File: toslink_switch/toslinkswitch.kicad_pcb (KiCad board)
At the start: 2 copper layers, 125.1 x 45.3 mm, 47 parts, among them IC1 ATMEGA48A-AU, IC2 SN74CBT3251, J1 CONN_02X03, J2 USB_OTG, SW2 INPUT_CYCL_SW, SW3 SW_DIP_x02

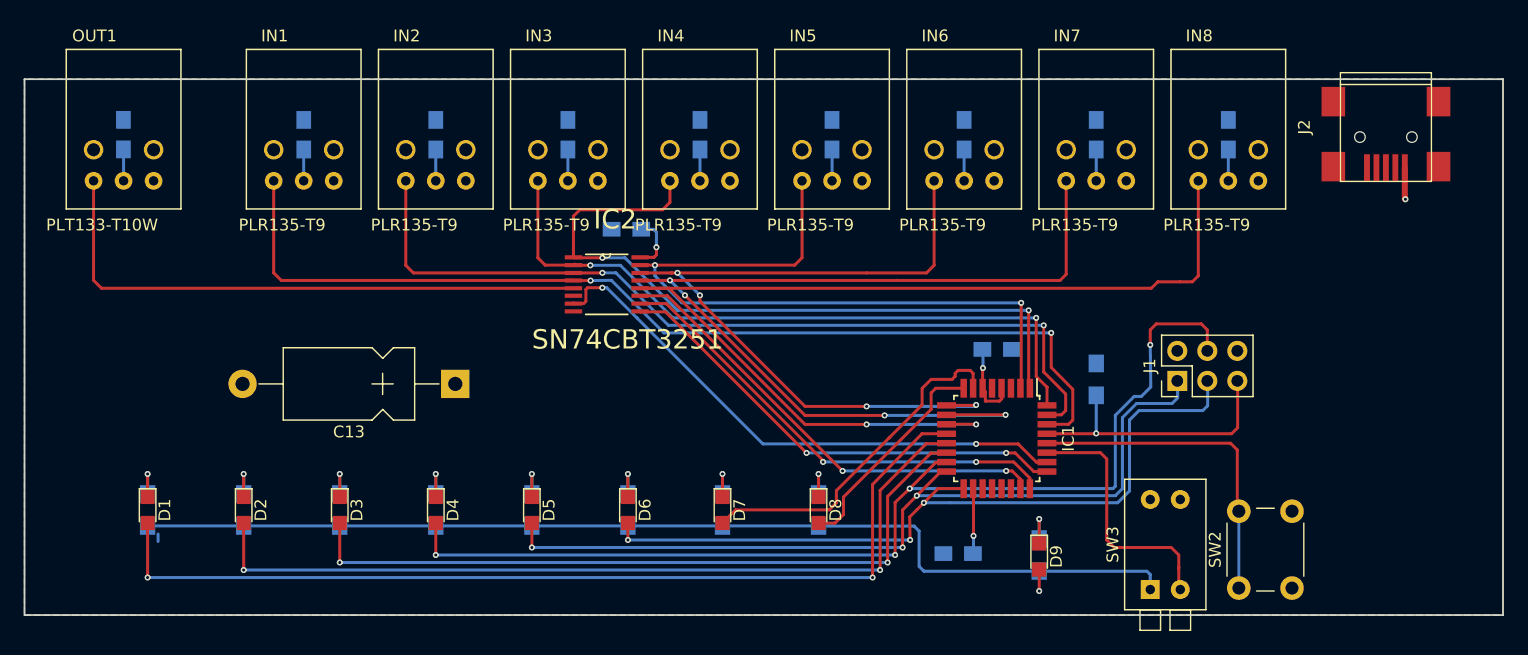
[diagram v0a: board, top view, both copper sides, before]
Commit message: add attiny for IR reciver functionality (https://blog.turboturbo.net/2016/10/01/ir-pc-power-on-quick-n-dirty/)
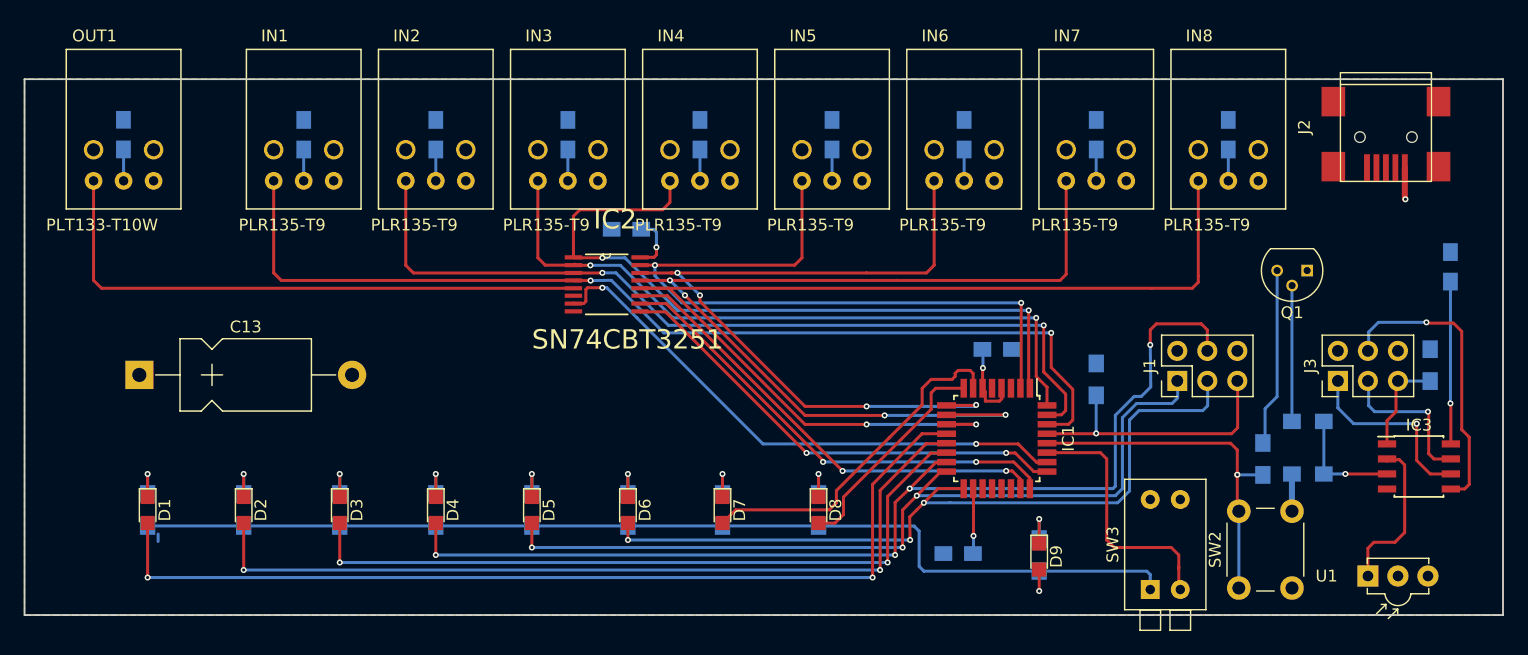
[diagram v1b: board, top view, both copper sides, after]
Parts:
- added C14: 100n, Capacitors_SMD:C_0805_HandSoldering, B.Cu at (181.4, 84.8)
- added IC3: ATTINY85-20SU, Housings_SOIC:SOIC-8_3.9x4.9mm_Pitch1.27mm, F.Cu at (178.7, 101.7)
- added J3: CONN_02X03, Pin_Headers:Pin_Header_Straight_2x03_Pitch2.54mm, F.Cu at (171.8, 94.5)
- added Q1: PN2222A, TO_SOT_Packages_THT:TO-92_Molded_Narrow, F.Cu at (169.2, 85.2)
- added R11: 47, Resistors_SMD:R_0805_HandSoldering, B.Cu at (169.3, 97.9)
- added R12: 47, Resistors_SMD:R_0805_HandSoldering, B.Cu at (165.5, 101.1)
- added R13: 1k, Resistors_SMD:R_0805_HandSoldering, B.Cu at (169.3, 102.4)
- added R14: 10k, Resistors_SMD:R_0805_HandSoldering, B.Cu at (179.6, 93.2)
- added U1: TSOP382xx, Opto-Devices:IRReceiver_Vishay_MINICAST-3pin, F.Cu at (174.4, 111.0)
- moved C13 26.7 mm to (70.4, 94.0), turned to 0 degrees
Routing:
- net Net-(IC3-Pad5): track 0.00 -> 25.1 mm, vias 0 -> 1
- net Net-(IC3-Pad6): track 0.00 -> 16.1 mm, vias 0 -> 1
- net Net-(Q1-Pad3): track 0.00 -> 15.2 mm
- net Net-(C14-Pad1): track 0.00 -> 13.8 mm, vias 0 -> 1
- net IR: track 0.00 -> 13.5 mm
- net Net-(IC3-Pad7): track 0.00 -> 13.1 mm, vias 0 -> 1
- net Net-(Q1-Pad2): track 0.00 -> 11.5 mm
- net IRSWSIG: track 0.00 -> 9.79 mm, vias 0 -> 1
- net Net-(IC3-Pad1): track 0.00 -> 8.57 mm
- net GND: track 0.34 -> 3.50 mm
- net TACT: track 28.1 -> 30.3 mm, vias 0 -> 1
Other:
- net class Default: trace_width 0.508 -> 0.254

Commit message: put some mounting holes where we still have space, we can cleanup later
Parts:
- added REF**: MountingHole_4mm, Mounting_Holes:MountingHole_4mm, F.Cu at (175.3, 82.9)
- added REF**: MountingHole_4mm, Mounting_Holes:MountingHole_4mm, F.Cu at (97.9, 93.5)
- added REF**: MountingHole_4mm, Mounting_Holes:MountingHole_4mm, F.Cu at (76.6, 82.2)
- added REF**: MountingHole_4mm, Mounting_Holes:MountingHole_4mm, F.Cu at (66.3, 108.0)
- added REF**: MountingHole_4mm, Mounting_Holes:MountingHole_4mm, F.Cu at (154.9, 82.7)
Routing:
- net (no net): track 0.64 -> 0.00 mm
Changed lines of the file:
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@@
     (links 128)
     (no_connects 0)
-    (area 60.630999 68.885999 185.876001 114.375001)
+    (area 60.630999 64.47 185.876001 115.966001)
     (thickness 1.6)
     (drawings 8)
-    (tracks 504)
+    (tracks 503)
     (zones 0)
-    (modules 56)
+    (modules 61)
     (nets 65)
   )
@@
       (net 42 VCC))
   )
+  (module Mounting_Holes:MountingHole_4mm (layer F.Cu)
+    (at 175.3235 82.931)
+    (descr "Mounting Hole 4mm, no annular")
+    (tags "mounting hole 4mm no annular")
+    (fp_text reference REF** (at 0 -5) (layer F.SilkS)
+      (effects (font (size 1 1) (thickness 0.15)))
+    )
+    (fp_text value MountingHole_4mm (at 0 5) (layer F.Fab)
+      (effects (font (size 1 1) (thickness 0.15)))
+    )
+    (fp_circle (center 0 0) (end 4 0) (layer Cmts.User) (width 0.15))
+    (fp_circle (center 0 0) (end 4.25 0) (layer F.CrtYd) (width 0.05))
+    (pad 1 np_thru_hole circle (at 0 0) (size 4 4) (drill 4) (layers *.Cu *.Mask))
+  )
+  (module Mounting_Holes:MountingHole_4mm (layer F.Cu)
+    (at 97.8535 93.5355)
+    (descr "Mounting Hole 4mm, no annular")
+    (tags "mounting hole 4mm no annular")
+    (fp_text reference REF** (at 0 -5) (layer F.SilkS)
+      (effects (font (size 1 1) (thickness 0.15)))
+    )
+    (fp_text value MountingHole_4mm (at 0 5) (layer F.Fab)
+      (effects (font (size 1 1) (thickness 0.15)))
+    )
+    (fp_circle (center 0 0) (end 4 0) (layer Cmts.User) (width 0.15))
+    (fp_circle (center 0 0) (end 4.25 0) (layer F.CrtYd) (width 0.05))
+    (pad 1 np_thru_hole circle (at 0 0) (size 4 4) (drill 4) (layers *.Cu *.Mask))
+  )
+  (module Mounting_Holes:MountingHole_4mm (layer F.Cu)
+    (at 76.581 82.169)
+    (descr "Mounting Hole 4mm, no annular")
+    (tags "mounting hole 4mm no annular")
+    (fp_text reference REF** (at 0 -5) (layer F.SilkS)
+      (effects (font (size 1 1) (thickness 0.15)))
+    )
+    (fp_text value MountingHole_4mm (at 0 5) (layer F.Fab)
+      (effects (font (size 1 1) (thickness 0.15)))
+    )
+    (fp_circle (center 0 0) (end 4 0) (layer Cmts.User) (width 0.15))
+    (fp_circle (center 0 0) (end 4.25 0) (layer F.CrtYd) (width 0.05))
+    (pad 1 np_thru_hole circle (at 0 0) (size 4 4) (drill 4) (layers *.Cu *.Mask))
+  )
+  (module Mounting_Holes:MountingHole_4mm (layer F.Cu)
+    (at 66.294 107.95)
+    (descr "Mounting Hole 4mm, no annular")
+    (tags "mounting hole 4mm no annular")
+    (fp_text reference REF** (at 0 -5) (layer F.SilkS)
+      (effects (font (size 1 1) (thickness 0.15)))
+    )
+    (fp_text value MountingHole_4mm (at 0 5) (layer F.Fab)
+      (effects (font (size 1 1) (thickness 0.15)))
+    )
+    (fp_circle (center 0 0) (end 4 0) (layer Cmts.User) (width 0.15))
+    (fp_circle (center 0 0) (end 4.25 0) (layer F.CrtYd) (width 0.05))
+    (pad 1 np_thru_hole circle (at 0 0) (size 4 4) (drill 4) (layers *.Cu *.Mask))
+  )
+  (module Mounting_Holes:MountingHole_4mm (layer F.Cu)
+    (at 154.94 82.677)
+    (descr "Mounting Hole 4mm, no annular")
+    (tags "mounting hole 4mm no annular")
+    (fp_text reference REF** (at 0 -5) (layer F.SilkS)
+      (effects (font (size 1 1) (thickness 0.15)))
+    )
+    (fp_text value MountingHole_4mm (at 0 5) (layer F.Fab)
+      (effects (font (size 1 1) (thickness 0.15)))
+    )
+    (fp_circle (center 0 0) (end 4 0) (layer Cmts.User) (width 0.15))
+    (fp_circle (center 0 0) (end 4.25 0) (layer F.CrtYd) (width 0.05))
+    (pad 1 np_thru_hole circle (at 0 0) (size 4 4) (drill 4) (layers *.Cu *.Mask))
+  )
   (gr_text https://circuit-board.de/forum/index.php/Thread/19096 (at 149.733 84.963) (layer B.Mask)
     (effects (font (size 1.5 1.5) (thickness 0.3)) (justify mirror))
@@
   (gr_line (start 60.706 68.961) (end 60.706 114.3) (angle 90) (layer Edge.Cuts) (width 0.15))
   (gr_line (start 185.801 68.961) (end 185.801 114.3) (angle 90) (layer Edge.Cuts) (width 0.15))
-  (segment (start 72.009 107.442) (end 72.009 108.077) (width 0.254) (layer B.Cu) (net 0))
   (segment (start 145.669 95.009) (end 145.669 88.519) (width 0.254) (layer F.Cu) (net 1))
   (segment (start 111.506 84.074) (end 115.951 88.519) (width 0.254) (layer B.Cu) (net 1))

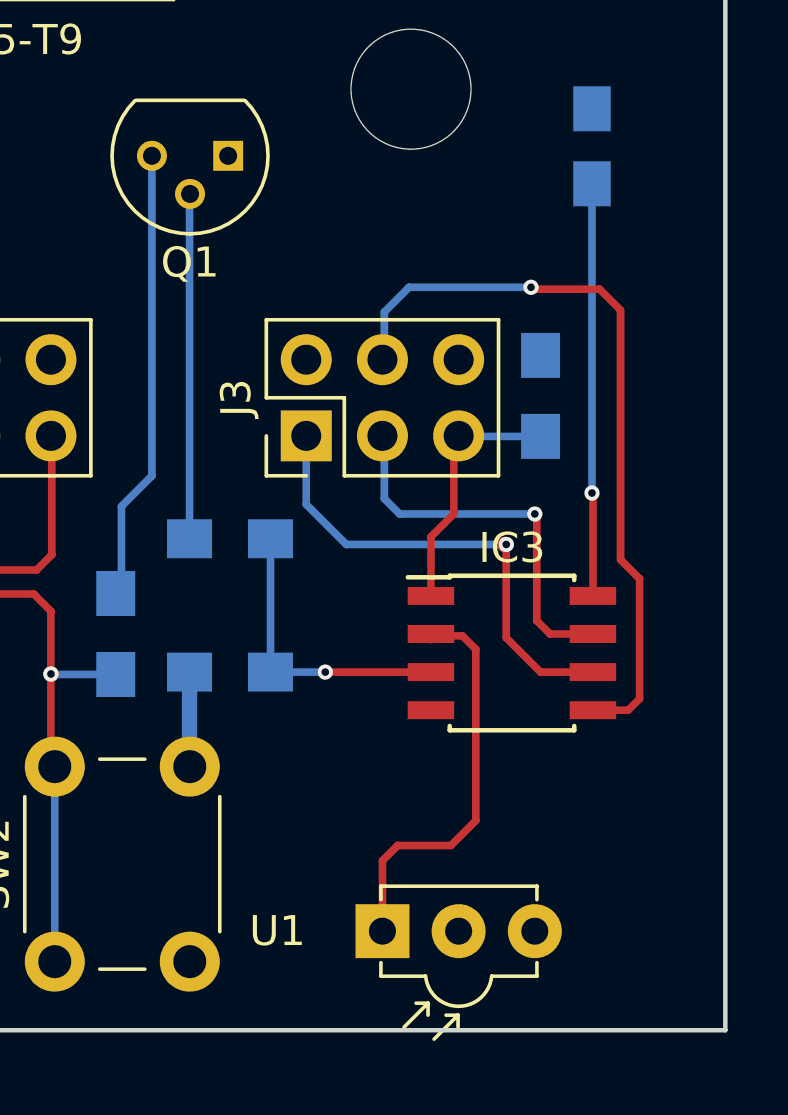
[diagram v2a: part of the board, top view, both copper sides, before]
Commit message: small tweaks to ic3 location
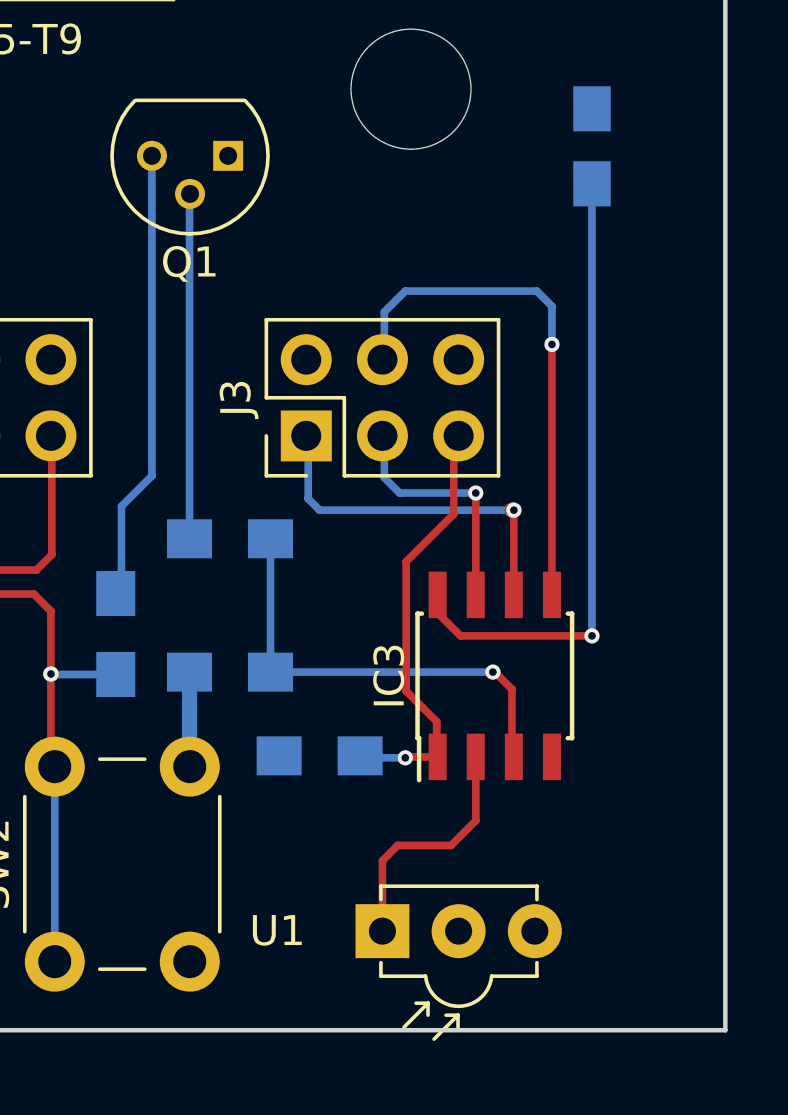
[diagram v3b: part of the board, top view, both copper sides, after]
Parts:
- moved R14 14.1 mm to (172.3, 105.2), turned to 180 degrees
- moved IC3 0.95 mm to (178.1, 102.5), turned to 90 degrees
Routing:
- net Net-(IC3-Pad5): track 25.1 -> 17.4 mm
- net Net-(C14-Pad1): track 13.8 -> 21.2 mm
- net Net-(IC3-Pad1): track 8.57 -> 14.8 mm, vias 0 -> 1
- net IR: track 13.5 -> 8.14 mm
- net IRSWSIG: track 9.79 -> 15.0 mm
- net Net-(IC3-Pad7): track 13.1 -> 8.31 mm
- net Net-(IC3-Pad6): track 16.1 -> 12.1 mm

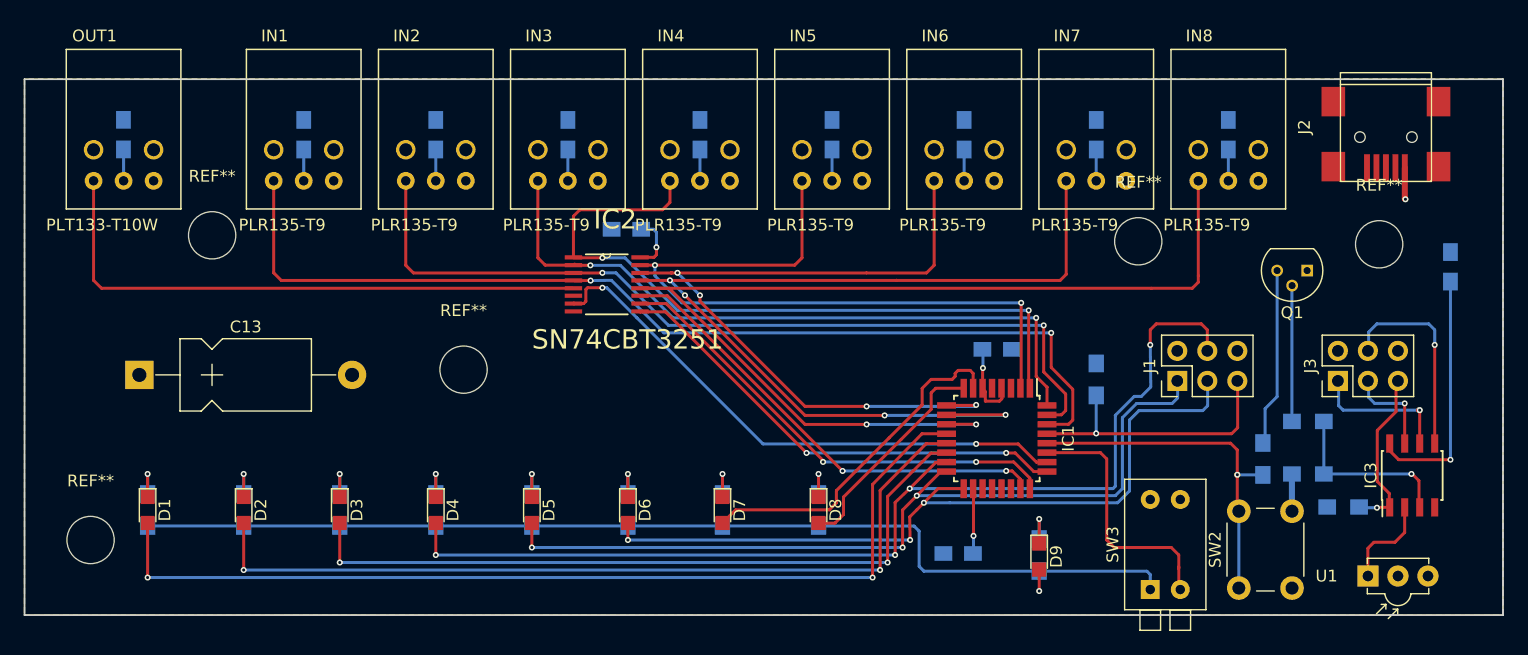
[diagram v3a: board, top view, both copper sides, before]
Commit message: move led's close to the edge of the board
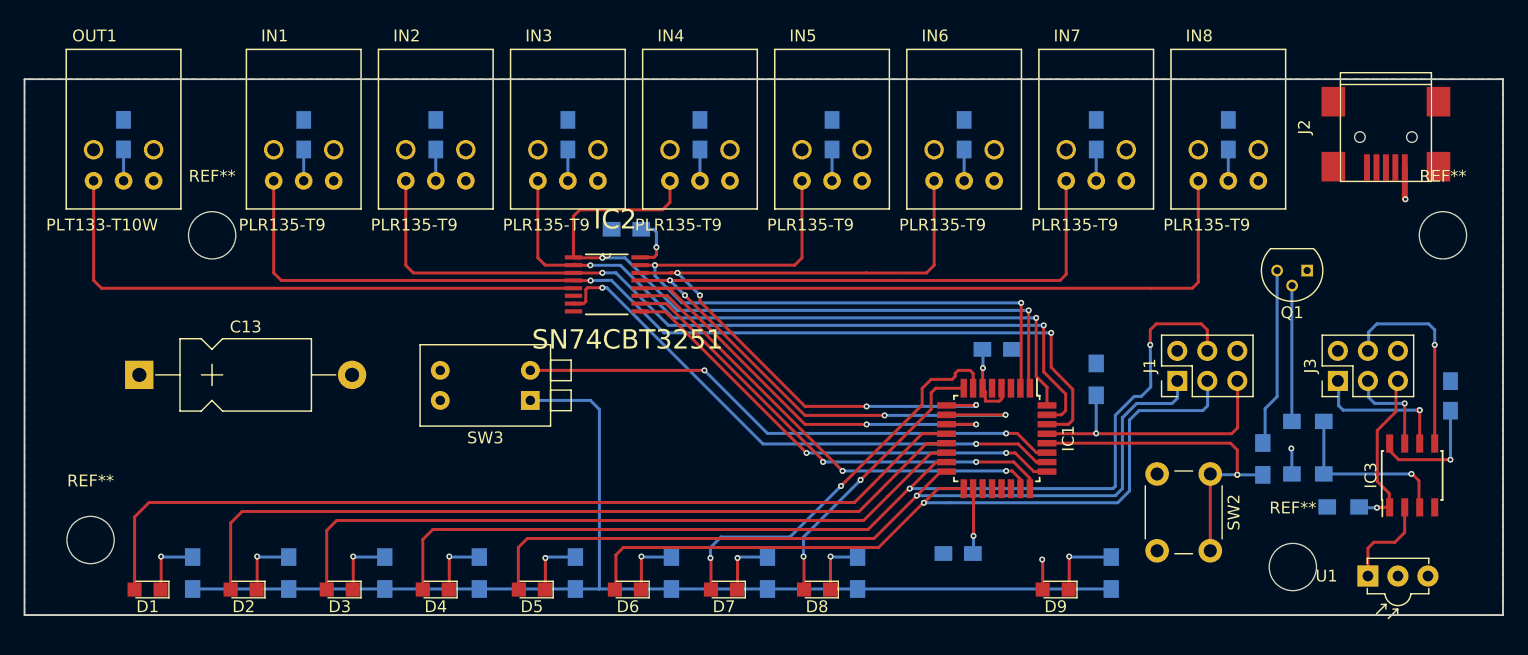
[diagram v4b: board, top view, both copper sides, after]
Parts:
- removed the REF** at (97.9, 93.5)
- moved SW3 54.8 mm to (103.5, 96.1), turned to 180 degrees
- moved REF** 30.5 mm to (168.0, 110.2)
- moved C14 10.9 mm to (181.4, 95.8)
- moved SW2 9.95 mm to (161.0, 102.4), turned to 270 degrees
- moved D7 6.73 mm to (119.9, 112.1), turned to 180 degrees
- moved D8 6.73 mm to (127.8, 112.1), turned to 180 degrees
- moved D1 6.73 mm to (71.1, 112.1), turned to 180 degrees
- moved D2 6.73 mm to (79.2, 112.1), turned to 180 degrees
- moved D3 6.73 mm to (87.4, 112.1), turned to 180 degrees
- moved D4 6.73 mm to (95.5, 112.1), turned to 180 degrees
- moved D5 6.73 mm to (103.6, 112.1), turned to 180 degrees
- moved D6 6.73 mm to (111.8, 112.1), turned to 180 degrees
- moved R1 6.55 mm to (74.9, 110.7)
- moved R2 6.55 mm to (83.1, 110.7)
- moved R3 6.55 mm to (91.2, 110.7)
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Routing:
- net DIP2: track 21.9 -> 46.6 mm, vias 0 -> 2
- net Net-(C14-Pad1): track 21.2 -> 10.2 mm
- net DIP1: track 89.6 -> 99.1 mm
- net LED8: track 18.7 -> 24.3 mm, vias 0 -> 2
- net LED7: track 29.6 -> 34.4 mm, vias 0 -> 2
- net LED1: track 82.0 -> 77.9 mm, vias 2 -> 0
- net Net-(D9-Pad1): track 3.77 -> 6.64 mm
- net LED2: track 72.0 -> 69.2 mm, vias 2 -> 0
- net LED6: track 65.9 -> 67.9 mm, vias 3 -> 1
- net Net-(D3-Pad1): track 3.65 -> 5.50 mm
- net Net-(D2-Pad1): track 3.65 -> 5.50 mm
- net Net-(D1-Pad1): track 3.65 -> 5.50 mm
- net Net-(D6-Pad1): track 3.65 -> 5.43 mm
- net Net-(D4-Pad1): track 3.65 -> 5.43 mm
- net Net-(D7-Pad1): track 3.65 -> 5.32 mm
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
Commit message: added ir indicator LED, rewrired tact switch to attiny instead of atmega, attiny will handle manual switching from now on. tact switch will provide manual switching on short press and IR code learning on >5 sec press
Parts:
- added D10: LED, LEDs:LED_0805, F.Cu at (148.0, 112.1)
- added R09: 330, Resistors_SMD:R_0805_HandSoldering, B.Cu at (152.7, 110.8)
- added R15: 330, Resistors_SMD:R_0805_HandSoldering, B.Cu at (144.5, 110.8)
- moved R14 23.5 mm to (151.4, 94.4), turned to 270 degrees
- moved R10 23.4 mm to (172.1, 105.2), turned to 180 degrees
- moved R9 18.0 mm to (134.7, 110.8)
- moved U1 17.7 mm to (156.7, 111.4)
- moved SW2 15.1 mm to (175.1, 107.9), turned to 0 degrees
- moved C14 9.18 mm to (173.0, 99.6)
- moved D9 7.05 mm to (140.9, 112.1)
- moved REF** 0.32 mm to (168.1, 109.9)
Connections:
- D9 pad 2: VCC -> LED9
- IC1 pad 28: TACT -> CYCLSW
- IC3 pad 6: Net-(IC3-Pad6) -> LED9
- IC3 pad 7: Net-(IC3-Pad7) -> TACT
- J3 pad 1: Net-(IC3-Pad6) -> LED9
- J3 pad 3: Net-(IC3-Pad7) -> TACT
- R10 pad 1: VCC -> Net-(IC3-Pad1)
- R10 pad 2: Net-(IC1-Pad29) -> VCC
- R12 pad 2: TACT -> CYCLSW
- R14 pad 1: Net-(IC3-Pad1) -> VCC
- R14 pad 2: VCC -> Net-(IC1-Pad29)
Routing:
- net LED9: track 0.00 -> 61.4 mm, vias 0 -> 3
- net IR: track 8.14 -> 32.1 mm
- net CYCLSW: track 0.00 -> 20.5 mm, vias 0 -> 1
- net Net-(IC3-Pad6): track 12.1 -> 0.00 mm, vias 1 -> 0
- net Net-(IC3-Pad7): track 8.31 -> 0.00 mm, vias 1 -> 0
- net Net-(D9-Pad1): track 6.64 -> 13.4 mm, vias 1 -> 2
- net Net-(D10-Pad1): track 0.00 -> 6.64 mm, vias 0 -> 1
- net TACT: track 29.4 -> 24.6 mm
- net Net-(C14-Pad1): track 10.2 -> 5.55 mm
